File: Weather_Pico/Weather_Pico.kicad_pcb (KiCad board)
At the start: 2 copper layers, 62 x 85 mm, 22 parts, among them J1 Pwr In, J2 12V, J3 Rain 3 Adv, J4 WIND, J5 RAIN 1, J6 Rain 2 Serial, J7 Debug, SW1 RUN, U1 Pico, U2 L7805

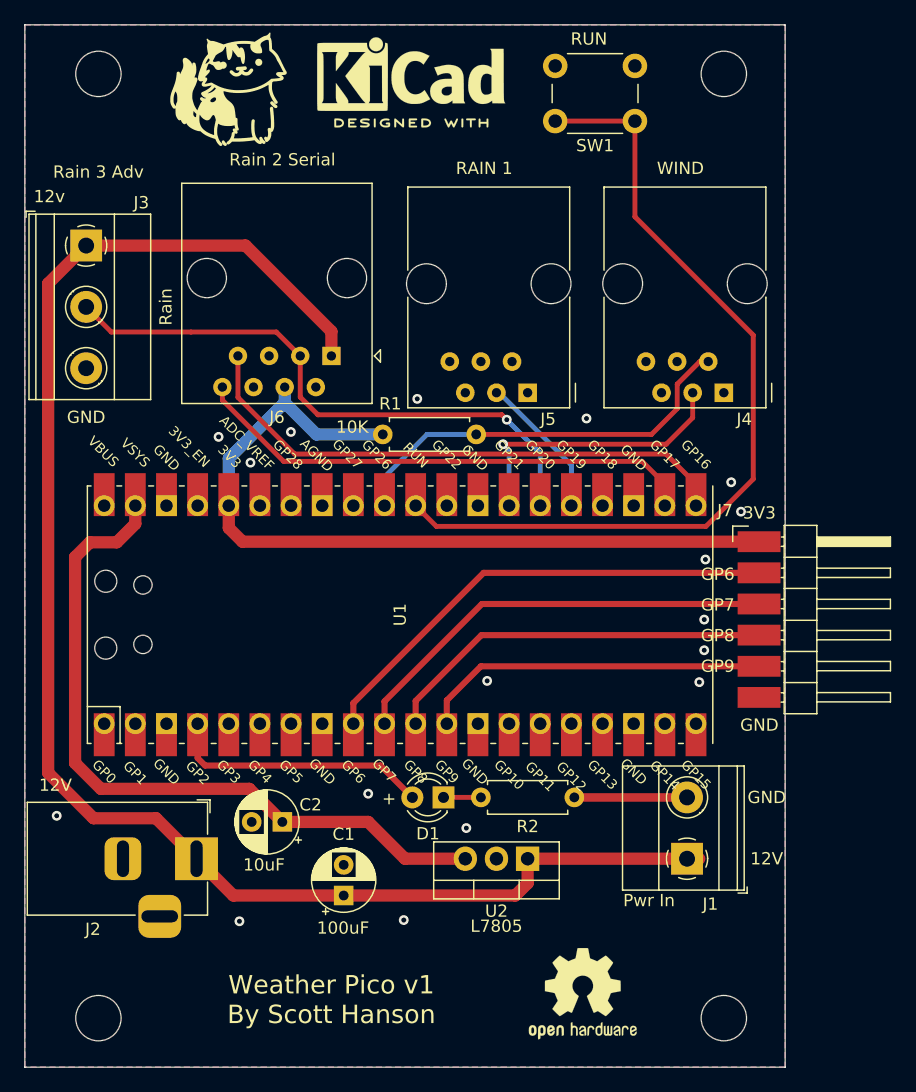
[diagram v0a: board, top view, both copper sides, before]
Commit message: added temperature headers
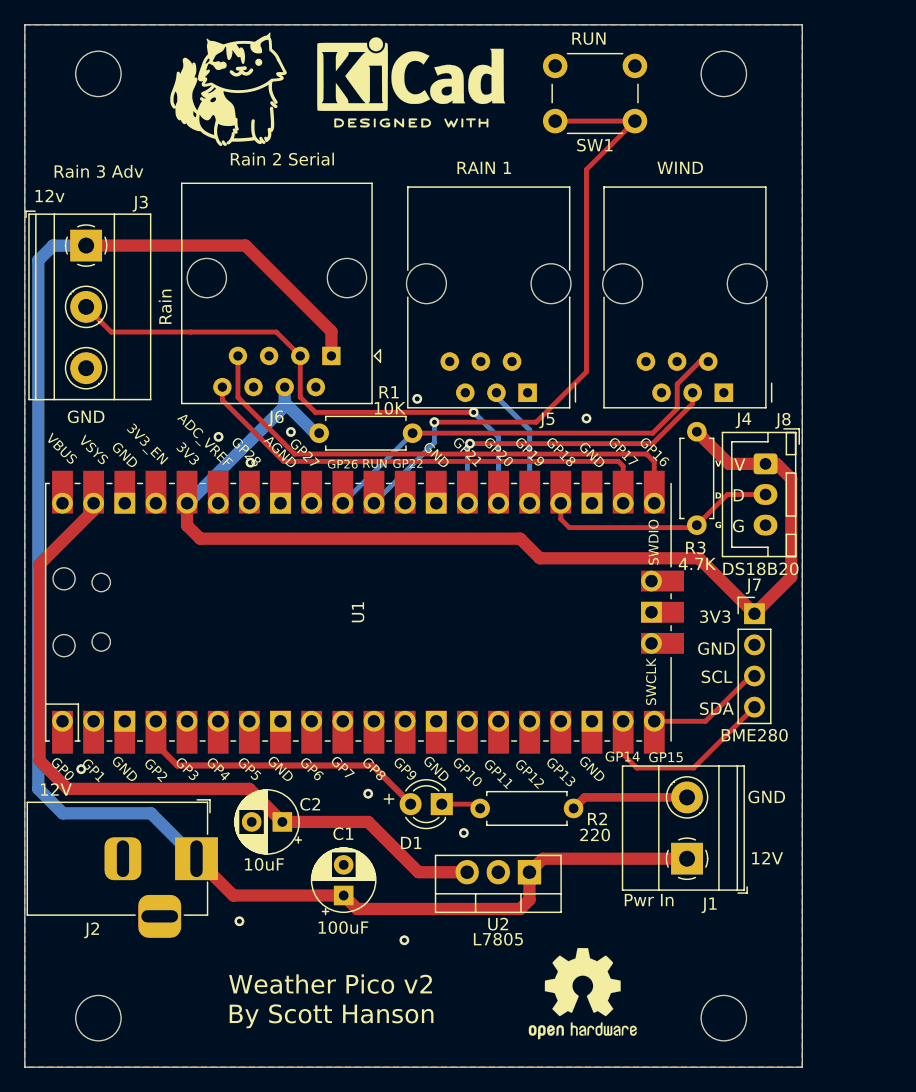
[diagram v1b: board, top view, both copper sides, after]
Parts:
- added J8: DS18B20, Connector_JST:JST_XH_B3B-XH-A_1x03_P2.50mm_Vertical, F.Cu at (179.4, 94.8)
- added R3: 4.7K, Resistor_THT:R_Axial_DIN0207_L6.3mm_D2.5mm_P7.62mm_Horizontal, F.Cu at (173.8, 99.8)
- J7: value Debug -> BME280; footprint Weather_Pico:1x06_Horizontal_SMD -> Connector_PinHeader_2.54mm:PinHeader_1x04_P2.54mm_Vertical
- U1: footprint MCU_RaspberryPi_and_Boards:RPi_Pico_SMD_TH_NO_DEBUG -> MCU_RaspberryPi_and_Boards:RPi_Pico_SMD_TH
- moved J7 8.51 mm to (178.5, 107.0)
- moved R1 5.19 mm to (143.0, 92.3)
- moved U1 3.41 mm to (146.2, 106.9)
- moved U2 1.11 mm to (160.2, 128.1)
- moved R2 0.90 mm to (163.8, 122.9)
- moved D1 0.57 mm to (153.0, 122.5)
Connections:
- J7 pad 2: Net-(J7-Pad2) -> GND
- J7 pad 3: Net-(J7-Pad3) -> SCL
- J7 pad 4: Net-(J7-Pad4) -> SDA
- U1 pad 10: Net-(J7-Pad3) -> unconnected-(U1-GPIO7-Pad10)
- U1 pad 11: Net-(J7-Pad4) -> unconnected-(U1-GPIO8-Pad11)
- U1 pad 12: Net-(J7-Pad5) -> unconnected-(U1-GPIO9-Pad12)
- U1 pad 19: unconnected-(U1-Pad19) -> SDA
- U1 pad 20: unconnected-(U1-Pad20) -> SCL
- U1 pad 24: unconnected-(U1-Pad24) -> 1-Wire
- U1 pad 9: Net-(J7-Pad2) -> unconnected-(U1-GPIO6-Pad9)
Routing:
- net Net-(J7-Pad2): track 40.1 -> 0.00 mm
- net Net-(J7-Pad3): track 36.6 -> 0.00 mm
- net Net-(J7-Pad4): track 33.0 -> 0.00 mm
- net Net-(J7-Pad5): track 29.4 -> 0.00 mm
- net +3V3: track 67.1 -> 89.3 mm
- net 1-Wire: track 0.00 -> 19.4 mm
- net Net-(U1-RUN): track 69.5 -> 51.3 mm, vias 0 -> 1
- net SDA: track 0.00 -> 15.9 mm
- net SCL: track 0.00 -> 9.70 mm
- net RAIN2: track 50.5 -> 45.4 mm
- net +12V: track 128.8 -> 132.4 mm
- net Net-(D1-A): track 21.6 -> 24.7 mm
- net TXD: track 41.7 -> 39.0 mm
- net RXD: track 45.4 -> 42.9 mm
- net +5V: track 59.4 -> 61.5 mm
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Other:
- board size 62 x 85 mm -> 63.4 x 85 mm
- board text added: "D"
- board text added: "G"
- board text added: "SCL"
- board text added: "SDA"
- board text added: "V"
- board text removed: "GP6"
- board text removed: "GP7"
- board text removed: "GP8"
- board text removed: "GP9"
